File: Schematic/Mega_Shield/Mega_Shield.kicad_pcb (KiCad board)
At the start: 2 copper layers, 102 x 71.8 mm, 17 parts, among them J1 Mini-DIN-4, J2 Conn_01x04_Female, J3 Mini-DIN-4, J4 Mini-DIN-4, J6 BLE HC-05, J7 MPU 6050, J8 NEO-6M, J9 SD_Card_Module, U1 ISL81487EIPZ

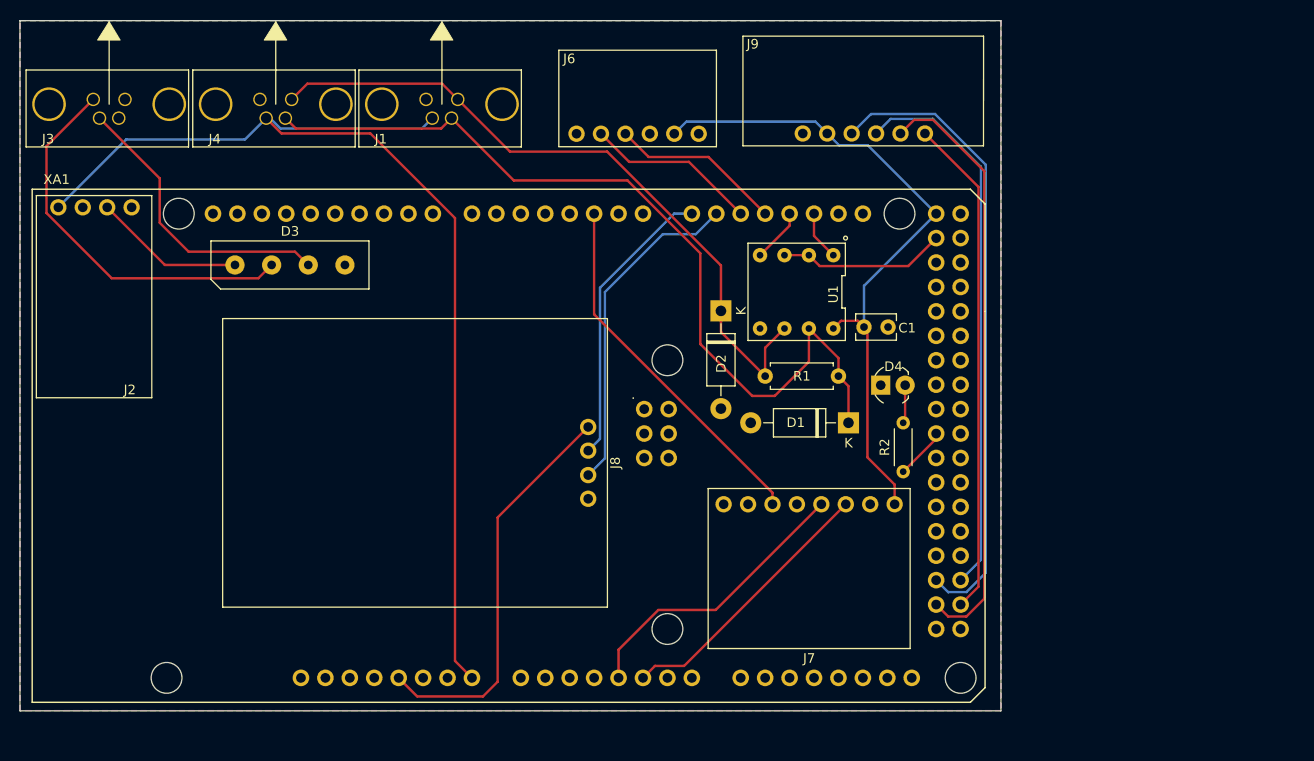
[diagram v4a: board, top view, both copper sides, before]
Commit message: Verion 4 PCB and Code
Updated PCB layout for version 4; for both TTS and Logger.
Updated code to asign ID to TTS and to send data via BT
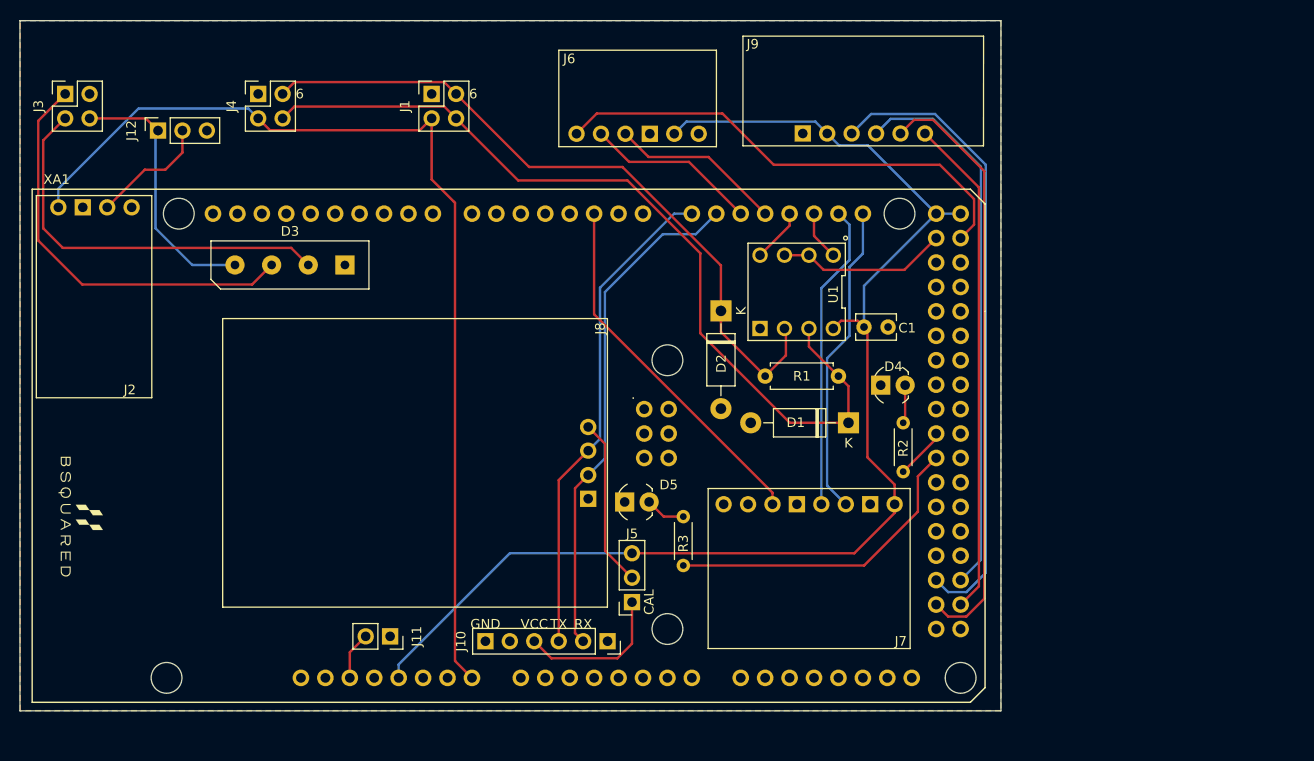
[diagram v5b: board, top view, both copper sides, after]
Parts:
- added D5: RED, Digikey:LED_3mm_Radial, F.Cu at (146.3, 67.8)
- added G***: LOGO, BSquared:BSquaredFP_12mm, B.Cu at (87.4, 69.3)
- added G***: LOGO, BSquared:BSquaredFP_12mm, F.Cu at (87.4, 69.3)
- added J10: Serial Reader, Connector_PinSocket_2.54mm:PinSocket_1x06_P2.54mm_Vertical, F.Cu at (142.0, 82.3)
- added J11: RESET SWT, Connector_PinSocket_2.54mm:PinSocket_1x02_P2.54mm_Vertical, F.Cu at (119.4, 81.8)
- added J12: Switch, Connector_PinSocket_2.54mm:PinSocket_1x03_P2.54mm_Vertical, F.Cu at (95.2, 29.2)
- added J5: Jumper, Connector_PinSocket_2.54mm:PinSocket_1x03_P2.54mm_Vertical, F.Cu at (144.5, 78.2)
- added R3: 4.7k, Resistor_THT:R_Axial_DIN0204_L3.6mm_D1.6mm_P5.08mm_Horizontal, F.Cu at (149.9, 74.4)
- J1, J3, J4: footprint TTS-URAT:RHT-634-1261-1 -> Connector_PinSocket_2.54mm:PinSocket_2x02_P2.54mm_Vertical
- moved J3 4.69 mm to (85.6, 25.4), turned to 90 degrees
- moved J4 2.12 mm to (105.7, 25.4), turned to 90 degrees
- moved J1 1.51 mm to (123.7, 25.4), turned to 90 degrees
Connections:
- net /A7 renamed Net-(XA1-PadA7)
- J2 pad 2: Net-(D3-Pad1) -> Net-(J12-Pad2)
- J3 pad 3: Net-(J3-Pad3) -> GND
- J3 pad 4: Net-(J3-Pad4) -> Net-(D3-Pad1)
- J6 pad 1: Net-(J6-Pad1) -> /D23
- J7 pad 5: /A4 -> /D20
- J7 pad 6: /A5 -> /D21
- J8 pad 1: VCC -> Net-(J5-Pad2)
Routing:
- net /D23: track 0.00 -> 50.5 mm
- net /D40: track 0.00 -> 33.1 mm
- net /D21: track 0.00 -> 32.6 mm
- net /D20: track 0.00 -> 31.9 mm
- net /A4: track 30.3 -> 0.00 mm
- net /A5: track 28.6 -> 0.00 mm
- net VCC: track 112.2 -> 133.4 mm
- net /D14: track 30.2 -> 51.3 mm
- net /D15: track 34.7 -> 52.9 mm
- net Net-(J5-Pad2): track 0.00 -> 17.6 mm
- net Net-(J10-Pad4): track 0.00 -> 15.8 mm
- net Net-(J12-Pad2): track 0.00 -> 12.5 mm
- net Net-(D3-Pad1): track 15.8 -> 27.7 mm
- net Net-(D3-Pad3): track 30.7 -> 41.5 mm
- net /VIN: track 116.1 -> 106.2 mm
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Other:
- board text added: "6"
- board text added: "CAL"
- board text added: "GND"
- board text added: "RX"
- board text added: "TX"
- board text added: "VCC"
